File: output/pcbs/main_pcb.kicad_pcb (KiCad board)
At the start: 2 copper layers, 153.5 x 109.7 mm, 28 parts

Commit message: Reverse keyswitches, reversible promicro
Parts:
- removed S26, S27: , PG1350
- removed xiao-ble1: ProMicro, xiao-ble
- added B1: Panasonic_EVQPUL_EVQPUC, Panasonic_EVQPUL_EVQPUC, F.Cu at (181.0, 86.2)
- added D1: , ComboDiode, F.Cu at (107.8, 153.5)
- added D10: , ComboDiode, F.Cu at (143.8, 118.5)
- added D11: , ComboDiode, F.Cu at (143.8, 101.5)
- added D12: , ComboDiode, F.Cu at (143.8, 84.5)
- added D13: , ComboDiode, F.Cu at (161.8, 141.5)
- added D14: , ComboDiode, F.Cu at (161.8, 124.5)
- added D15: , ComboDiode, F.Cu at (161.8, 107.5)
- added D16: , ComboDiode, F.Cu at (161.8, 90.5)
- added D17: , ComboDiode, F.Cu at (179.8, 143.5)
- added D18: , ComboDiode, F.Cu at (179.8, 126.5)
- added D19: , ComboDiode, F.Cu at (179.8, 109.5)
- added D2: , ComboDiode, F.Cu at (107.8, 136.5)
- added D20: , ComboDiode, F.Cu at (179.8, 92.5)
- added D21: , ComboDiode, F.Cu at (89.8, 134.5)
- added D22: , ComboDiode, F.Cu at (89.8, 117.5)
- added D23: , ComboDiode, F.Cu at (169.8, 162.5)
- added D24: , ComboDiode, F.Cu at (191.5, 168.9)
- added D25: , ComboDiode, F.Cu at (211.2, 178.6)
- added D3: , ComboDiode, F.Cu at (107.8, 119.5)
- added D4: , ComboDiode, F.Cu at (107.8, 102.5)
- added D5: , ComboDiode, F.Cu at (125.8, 141.5)
- added D6: , ComboDiode, F.Cu at (125.8, 124.5)
- added D7: , ComboDiode, F.Cu at (125.8, 107.5)
- added D8: , ComboDiode, F.Cu at (125.8, 90.5)
- added D9: , ComboDiode, F.Cu at (143.8, 135.5)
- added JST1: , JST_PH_S2B-PH-K_02x2.00mm_Angled, F.Cu at (165.0, 117.5)
- added LED1: , WS2812B,  at (100.0, 155.0)
- added LED10: , WS2812B,  at (136.0, 120.0)
- added LED11: , WS2812B,  at (136.0, 103.0)
- added LED12: , WS2812B,  at (136.0, 86.0)
- added LED13: , WS2812B,  at (154.0, 143.0)
- added LED14: , WS2812B,  at (154.0, 126.0)
- added LED15: , WS2812B,  at (154.0, 109.0)
- added LED16: , WS2812B,  at (154.0, 92.0)
- added LED17: , WS2812B,  at (172.0, 145.0)
- added LED18: , WS2812B,  at (172.0, 128.0)
- added LED19: , WS2812B,  at (172.0, 111.0)
- added LED2: , WS2812B,  at (100.0, 138.0)
- added LED20: , WS2812B,  at (172.0, 94.0)
- added LED21: , WS2812B,  at (82.0, 136.0)
- added LED22: , WS2812B,  at (82.0, 119.0)
- added LED23: , WS2812B,  at (162.0, 164.0)
- added LED24: , WS2812B,  at (183.6, 167.9)
- added LED25: , WS2812B,  at (203.6, 176.3)
- added LED3: , WS2812B,  at (100.0, 121.0)
- added LED4: , WS2812B,  at (100.0, 104.0)
- added LED5: , WS2812B,  at (118.0, 143.0)
- added LED6: , WS2812B,  at (118.0, 126.0)
- added LED7: , WS2812B,  at (118.0, 109.0)
- added LED8: , WS2812B,  at (118.0, 92.0)
- added LED9: , WS2812B,  at (136.0, 137.0)
- added MCU1: , ceoloide:mcu_supermini_nrf52840, F.Cu at (156.0, 90.5)
- moved S24 252.8 mm to (185.2, 163.1), turned to -18 degrees
- moved S23 224.0 mm to (162.0, 159.0), turned to 0 degrees
- moved S25 211.2 mm to (205.9, 171.9), turned to -28 degrees
- moved S16 192.4 mm to (154.0, 87.0), turned to 0 degrees
- moved S15 191.7 mm to (154.0, 104.0), turned to 0 degrees
- moved S14 190.9 mm to (154.0, 121.0), turned to 0 degrees
- moved S13 190.2 mm to (154.0, 138.0), turned to 0 degrees
- moved S20 190.2 mm to (172.0, 89.0), turned to 0 degrees
- moved S19 189.4 mm to (172.0, 106.0), turned to 0 degrees
- moved S18 188.6 mm to (172.0, 123.0), turned to 0 degrees
- moved S17 187.9 mm to (172.0, 140.0), turned to 0 degrees
- moved S4 182.6 mm to (100.0, 99.0), turned to 0 degrees
- moved S3 181.8 mm to (100.0, 116.0), turned to 0 degrees
- moved S2 181.1 mm to (100.0, 133.0), turned to 0 degrees
- moved S12 180.9 mm to (136.0, 81.0), turned to 0 degrees
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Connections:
- S1 pad 1: (no net) -> P1
- S1 pad 2: outer_bottom -> pinky_bottom
- S10 pad 1: (no net) -> P3
- S10 pad 2: ring_home -> middle_home
- S11 pad 1: (no net) -> P3
- S11 pad 2: ring_top -> middle_top
- S12 pad 1: (no net) -> P3
- S12 pad 2: ring_num -> middle_num
- S13 pad 1: (no net) -> P4
- S13 pad 2: middle_bottom -> index_bottom
- S14 pad 1: (no net) -> P4
- S14 pad 2: middle_home -> index_home
- S15 pad 1: (no net) -> P4
- S15 pad 2: middle_top -> index_top
- S16 pad 1: (no net) -> P4
- S16 pad 2: middle_num -> index_num
- S17 pad 1: (no net) -> P5
- S17 pad 2: index_bottom -> inner_bottom
- S18 pad 1: (no net) -> P5
- S18 pad 2: index_home -> inner_home
- S19 pad 1: (no net) -> P5
- S19 pad 2: index_top -> inner_top
- S2 pad 1: (no net) -> P1
- S2 pad 2: outer_home -> pinky_home
- S20 pad 1: (no net) -> P5
- S20 pad 2: index_num -> inner_num
- S21 pad 1: (no net) -> P0
- S21 pad 2: inner_bottom -> outer_top
- S22 pad 1: (no net) -> P0
- S22 pad 2: inner_home -> outer_home
- S23 pad 1: (no net) -> P3
- S23 pad 2: inner_top -> near_thumb
- S24 pad 1: (no net) -> P4
- S24 pad 2: inner_num -> home_thumb
- S25 pad 1: (no net) -> P5
- S25 pad 2: near_thumb -> far_thumb
- S3 pad 1: (no net) -> P1
- S3 pad 2: outer_top -> pinky_top
- S4 pad 1: (no net) -> P1
- S4 pad 2: outer_num -> pinky_num
- S5 pad 1: (no net) -> P2
- S5 pad 2: pinky_bottom -> ring_bottom
- S6 pad 1: (no net) -> P2
- S6 pad 2: pinky_home -> ring_home
- S7 pad 1: (no net) -> P2
- S7 pad 2: pinky_top -> ring_top
- S8 pad 1: (no net) -> P2
- S8 pad 2: pinky_num -> ring_num
- S9 pad 1: (no net) -> P3
- S9 pad 2: ring_bottom -> middle_bottom
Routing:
- net (no net): track 0.00 -> 337.7 mm
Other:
- board size 153.5 x 109.7 mm -> 147.5 x 112.7 mm
- net class Default added: clearance 0.2, trace_width 0.25, via_dia 0.8, via_drill 0.4
- board text added: "by karl ryberg"
- board text added: "hormesis"

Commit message: Positions determined (more or less)
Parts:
- added H1: , mounting_hole, F.Cu at (217.5, 168.0)
- added H2: , mounting_hole, F.Cu at (179.5, 76.0)
- added H3: , mounting_hole, F.Cu at (89.0, 157.0)
- added H4: , mounting_hole, F.Cu at (74.5, 143.0)
- added H5: , mounting_hole, F.Cu at (173.0, 168.0)
- added H6: , mounting_hole, F.Cu at (133.0, 157.0)
- added H7: , mounting_hole, F.Cu at (111.0, 112.5)
- added H8: , mounting_hole, F.Cu at (165.0, 133.5)
- added H9: , mounting_hole, F.Cu at (71.0, 76.0)
- added SW1: , power_switch, F.Cu at (113.0, 74.8)
- moved B1 85.2 mm to (96.5, 75.4), turned to 0 degrees
- moved MCU1 74.3 mm to (81.7, 90.2), turned to 0 degrees
- moved JST1 36.8 mm to (169.5, 81.0)
- moved D13 4.00 mm to (161.8, 145.5)
- moved D14 4.00 mm to (161.8, 128.5)
- moved D15 4.00 mm to (161.8, 111.5)
- moved D16 4.00 mm to (161.8, 94.5)
- moved D17 4.00 mm to (179.8, 147.5)
- moved D18 4.00 mm to (179.8, 130.5)
- moved D19 4.00 mm to (179.8, 113.5)
- moved D20 4.00 mm to (179.8, 96.5)
- moved LED13 4.00 mm to (154.0, 147.0)
- moved LED14 4.00 mm to (154.0, 130.0)
- moved LED15 4.00 mm to (154.0, 113.0)
- moved LED16 4.00 mm to (154.0, 96.0)
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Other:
- board size 147.5 x 112.7 mm -> 150.9 x 112.7 mm

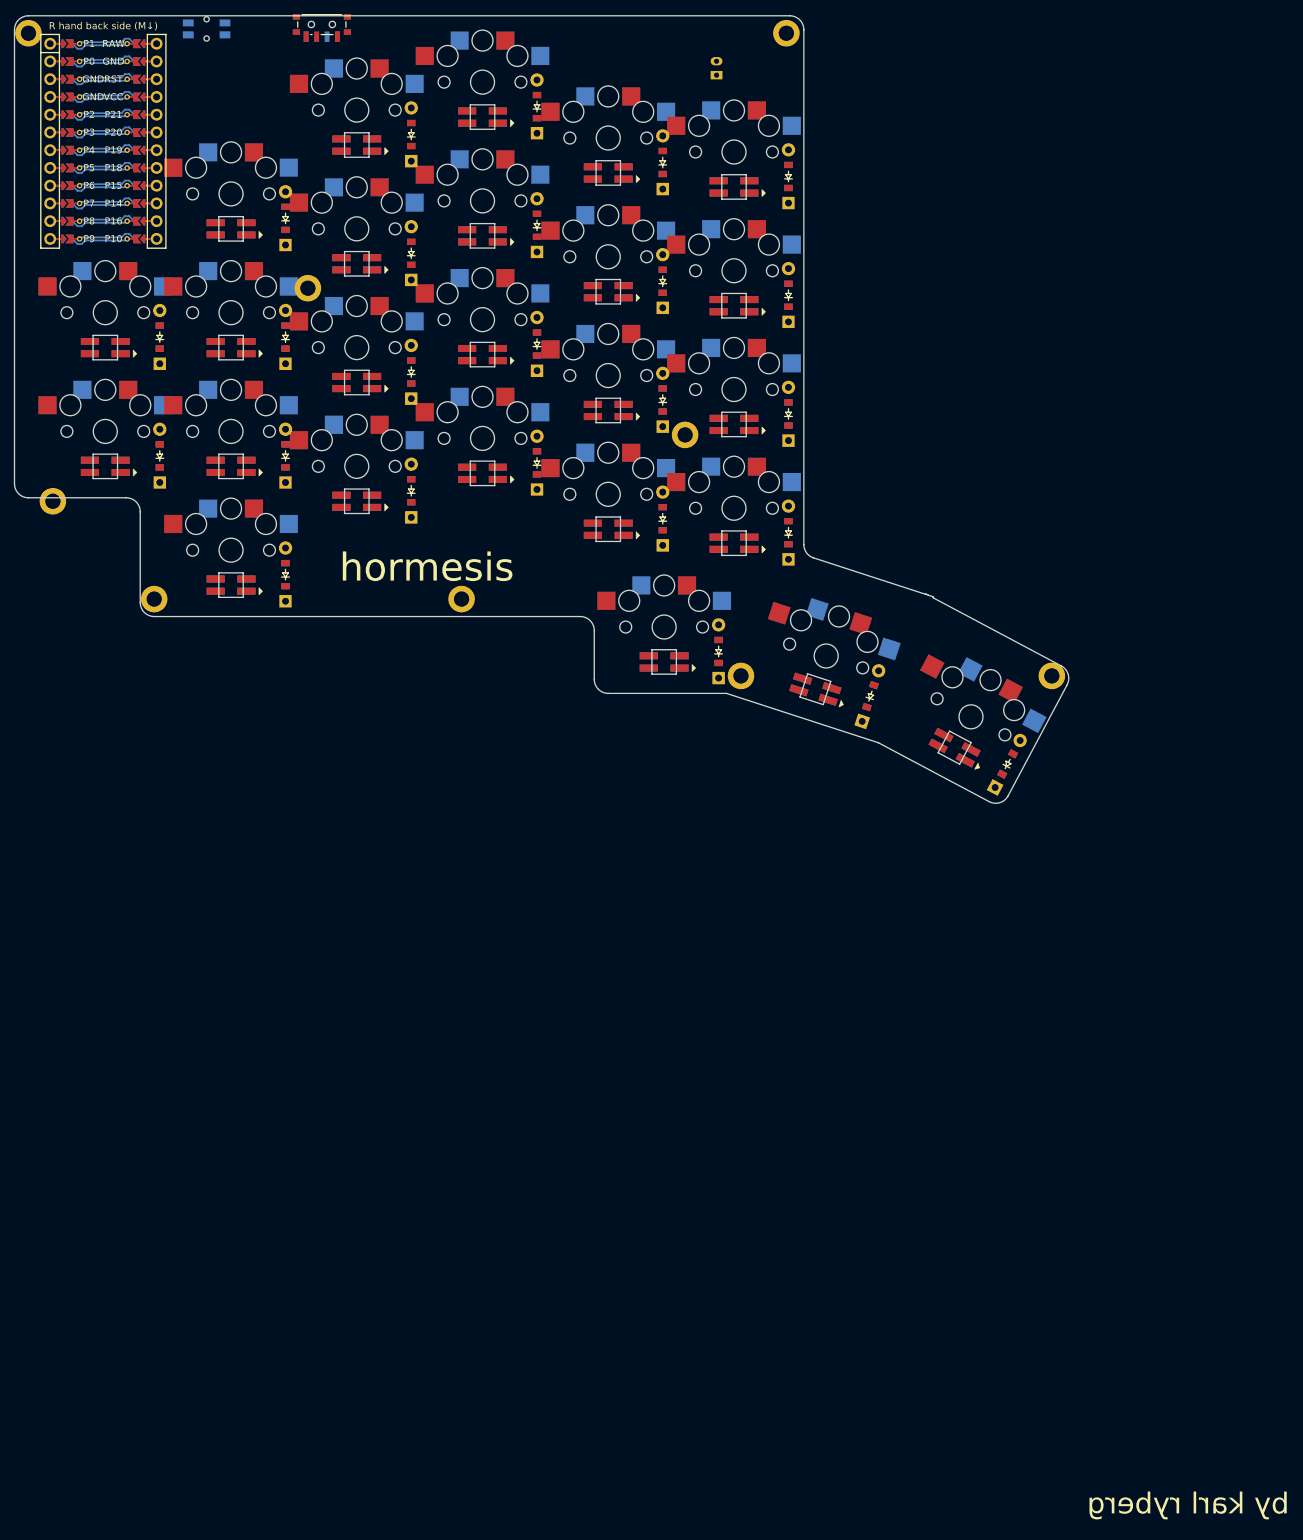
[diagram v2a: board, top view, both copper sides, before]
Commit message: Remove mounting holes & prepare ergogen for routing
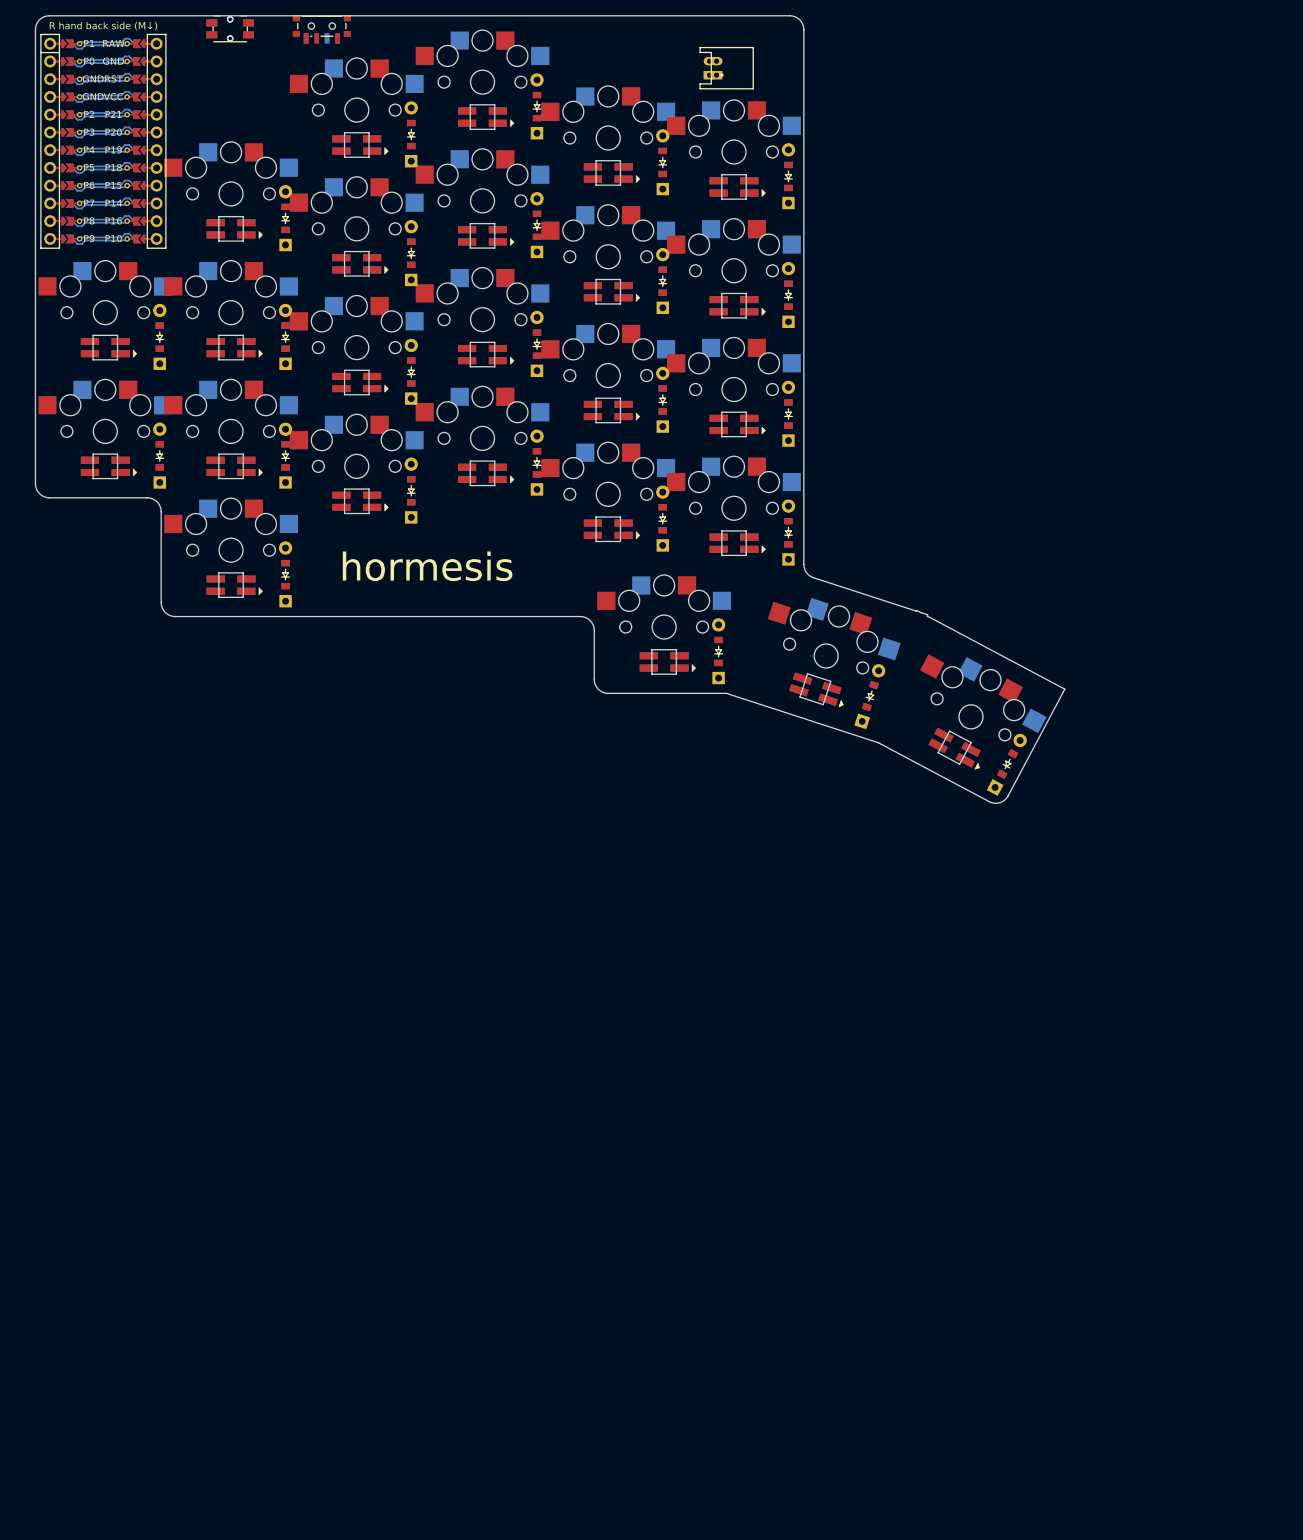
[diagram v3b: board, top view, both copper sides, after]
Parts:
- removed H1, H2, H3, H4, H5, H6, H7, H8, H9: , mounting_hole
- added B2: Panasonic_EVQPUL_EVQPUC, Panasonic_EVQPUL_EVQPUC, F.Cu at (99.9, 75.4)
- added JST2: , JST_PH_S2B-PH-K_02x2.00mm_Angled, F.Cu at (168.5, 81.0)
- moved B1 3.38 mm to (99.9, 75.4)
- moved SW1 0.23 mm to (113.0, 75.0)
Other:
- board size 150.9 x 112.7 mm -> 147.4 x 112.7 mm

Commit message: Adjust positions
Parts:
- moved JST2 3.64 mm to (167.5, 77.5)
- moved JST1 3.54 mm to (170.0, 77.5)
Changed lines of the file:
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@@
                 (effects (font (size 4 4) (thickness 0.5) ) (justify left))
             )
-            (gr_text "by karl ryberg" (at 150 152.5 0) (layer B.SilkS)
+            (gr_text "by karl ryberg" (at 145 152.5 0) (layer B.SilkS)
                 (effects (font (size 3 3) (thickness 0.4) ) (justify mirror left))
             )
@@
         (descr "JST PH series connector, S2B-PH-K, side entry type, through hole, Datasheet: http://www.jst-mfg.com/product/pdf/eng/ePH.pdf")
         (tags "connector jst ph")
-        (at 169.5 81 90)
+        (at 170 77.5 90)
         (fp_text reference "JST1" (at 0 0) (layer F.SilkS) hide (effects (font (size 1.27 1.27) (thickness 0.15))))
         (fp_text value "" (at 0 0) (layer F.SilkS) hide (effects (font (size 1.27 1.27) (thickness 0.15))))
@@
         (descr "JST PH series connector, S2B-PH-K, side entry type, through hole, Datasheet: http://www.jst-mfg.com/product/pdf/eng/ePH.pdf")
         (tags "connector jst ph")
-        (at 168.5 81 90)
+        (at 167.5 77.5 90)
         (fp_text reference "JST2" (at 0 0) (layer F.SilkS) hide (effects (font (size 1.27 1.27) (thickness 0.15))))
         (fp_text value "" (at 0 0) (layer F.SilkS) hide (effects (font (size 1.27 1.27) (thickness 0.15))))
